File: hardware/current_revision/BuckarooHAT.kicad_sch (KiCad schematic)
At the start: 15 parts, among them J1 +12V PoE In, J2 Raspberry Pi Power In, J3 GEC03SBSN-M89, U1 AP62301WU

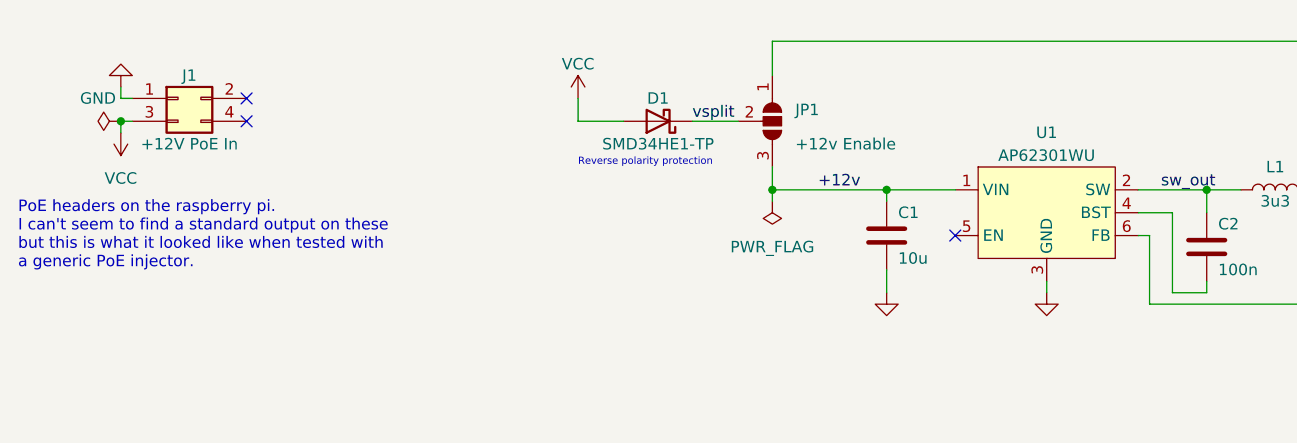
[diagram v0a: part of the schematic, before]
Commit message: Fixed footprint for buck
How did this happen???
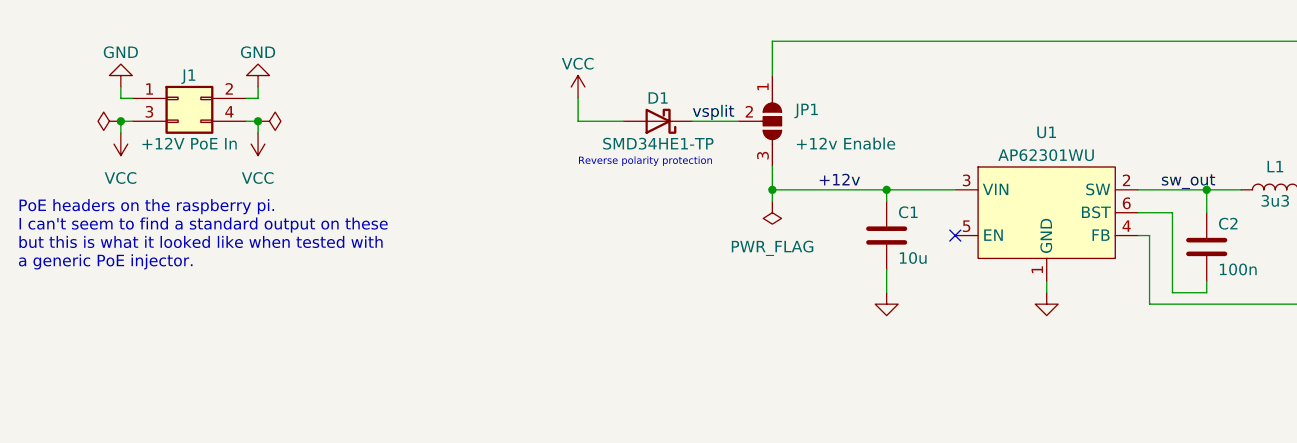
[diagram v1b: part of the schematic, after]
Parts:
- U1: ID AP62301WU -> (none)
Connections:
- net +12v: now also U1.3 (VIN); no longer U1.1 (VIN)
- net GND: now also J1.2 (Pin_2), U1.1 (GND); no longer U1.3 (GND)
- net VCC: now also J1.4 (Pin_4)
- net fb_in: now also U1.4 (FB); no longer U1.6 (FB)
- net at C2.2: now also U1.6 (BST); no longer U1.4 (BST)
- no-connect marks 5 -> 3
